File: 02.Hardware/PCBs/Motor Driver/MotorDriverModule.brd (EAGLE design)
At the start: 62 x 62 mm, 45 parts, among them Q1 DMC3021LSD-13, Q2 DMC3021LSD-13, Q3 DMC3021LSD-13, U1 FAN3268TMX, U2 FAN3268TMX, U3 FAN3268TMX, U4 MCP6001T-I_LT

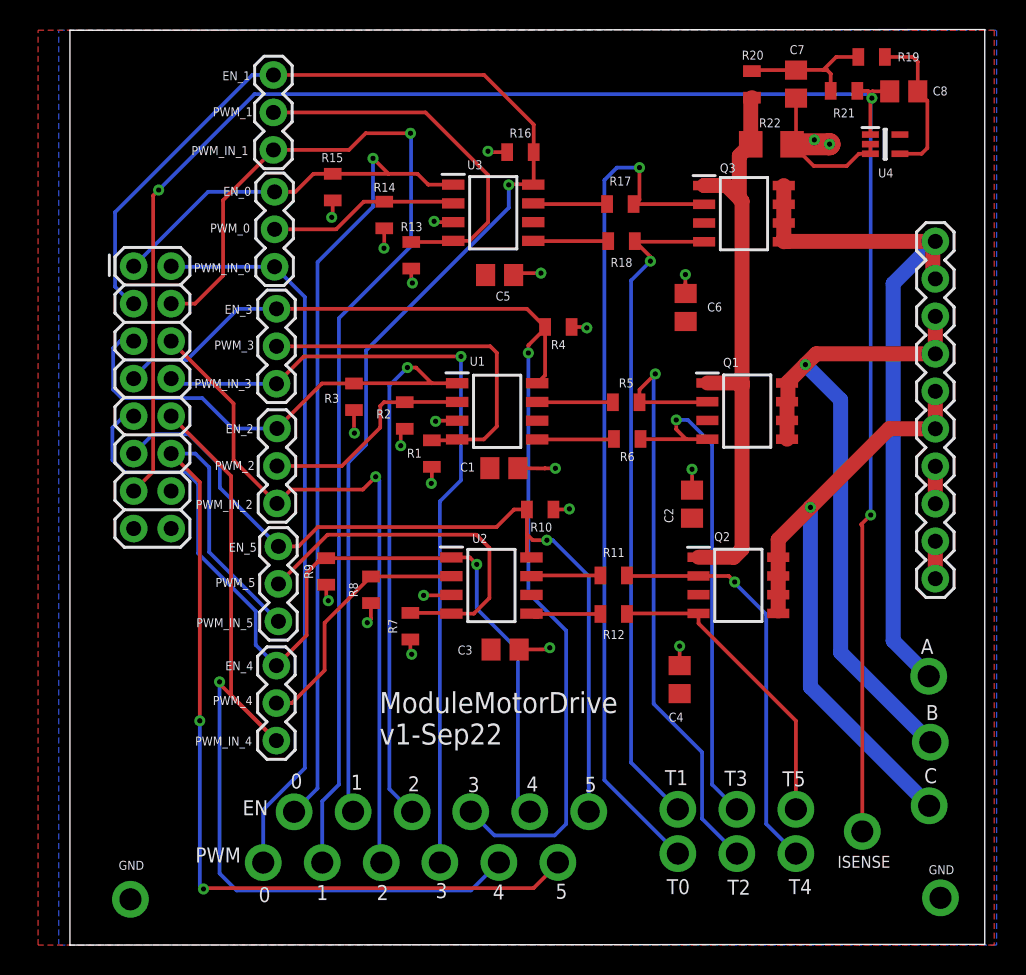
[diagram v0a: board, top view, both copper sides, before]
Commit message: Cambios de rutado y nombres
Cambios de rutado y nombres
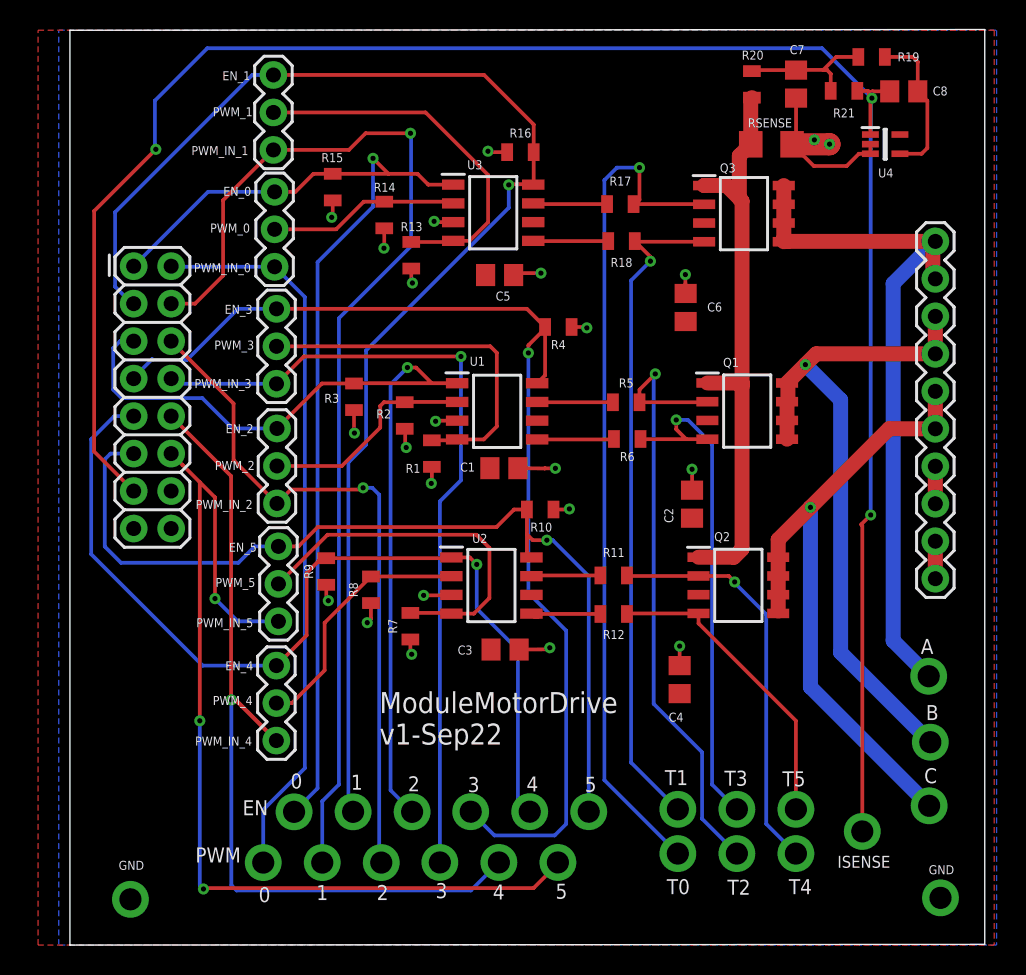
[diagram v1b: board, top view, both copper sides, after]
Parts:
- renumbered R22 to RSENSE
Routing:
- net ISENSE: track 127.9 -> 136.4 mm
- net EN_5: track 57.0 -> 63.3 mm
- net PWM_IN_4: track 63.7 -> 60.9 mm
- net PWM_IN_5: track 70.6 -> 68.5 mm, vias 3 -> 4
- net EN_4: track 62.5 -> 64.5 mm
- net PWM_IN_2: track 47.7 -> 46.5 mm

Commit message: v2 Cambio de conector de entrada y correccion de errores
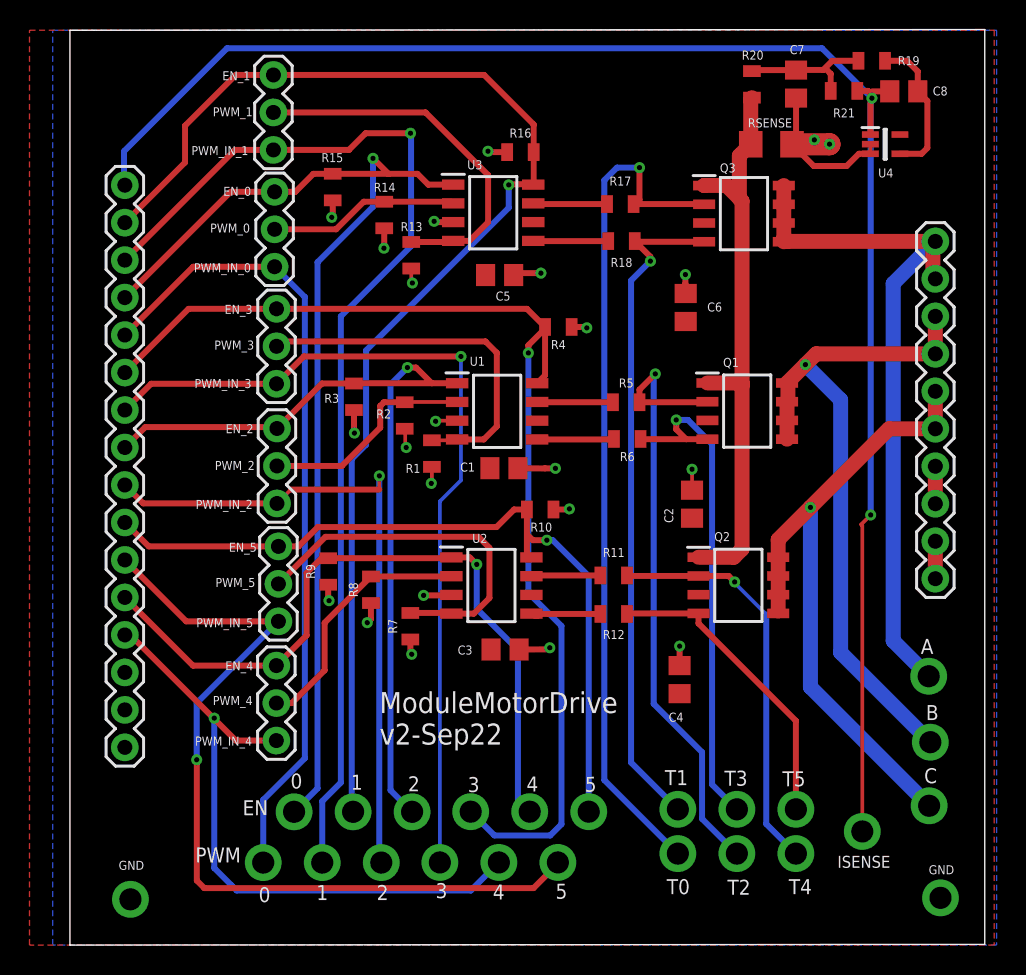
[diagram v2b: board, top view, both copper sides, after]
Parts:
- J1: device SparkFun-Connectors:2X8 -> SparkFun-Connectors:1X16
- moved J1 5.52 mm to (12.5, 58.3)
- moved R19 0.26 mm to (63.1, 66.7)
- moved R9 0.13 mm to (26.3, 32.1)
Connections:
- removed net N$27: J1.14
- net EN_0: now also J1.4; no longer J1.1
- net EN_1: now also J1.2; no longer J1.3
- net EN_2: now also J1.8; no longer J1.5
- net EN_3: now also J1.6; no longer J1.7
- net EN_4: now also J1.12; no longer J1.9
- net EN_5: now also J1.10; no longer J1.11
- net GND: now also J1.14, J1.15; no longer J1.16
- net ISENSE: now also J1.1; no longer J1.13
- net PWM_IN_0: now also J1.5; no longer J1.2
- net PWM_IN_1: now also J1.3; no longer J1.4
- net PWM_IN_2: now also J1.9; no longer J1.6
- net PWM_IN_3: now also J1.7; no longer J1.8
- net PWM_IN_4: now also J1.13; no longer J1.10
- net PWM_IN_5: now also J1.11; no longer J1.12
- net VCC: now also J1.16; no longer J1.15
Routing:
- net ISENSE: track 136.4 -> 112.9 mm, vias 4 -> 3
- net PWM_IN_4: track 60.9 -> 44.3 mm
- net EN_4: track 64.5 -> 49.7 mm
- net PWM_IN_5: track 68.5 -> 57.5 mm, vias 4 -> 2
- net EN_5: track 63.3 -> 53.7 mm
- net EN_1: track 93.3 -> 87.7 mm
- net EN_2: track 63.3 -> 57.7 mm
- net PWM_IN_0: track 49.4 -> 54.5 mm
- net PWM_IN_3: track 55.4 -> 59.2 mm
- net EN_0: track 72.5 -> 74.2 mm
- net PWM_IN_2: track 46.5 -> 45.4 mm
- net PWM_IN_1: track 75.9 -> 74.9 mm
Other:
- board text added: "ModuleMotorDrive v2-Sep22"
- board text removed: "ModuleMotorDrive v1-Sep22"

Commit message: Minor modifications
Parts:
- added C9: (no value), rcl:C0805
- moved R9 0.64 mm to (26.9, 32.2)
- moved R8 0.16 mm to (29.4, 30.9)
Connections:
- net GND: now also C9.2
- net VCC: now also C9.1
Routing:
- net A_OUT: track 59.9 -> 74.5 mm, vias 1 -> 4
- net B_OUT: track 46.4 -> 56.2 mm, vias 2 -> 4
- net EN_2: track 57.7 -> 54.7 mm
- net EN_3: track 76.9 -> 74.9 mm, vias 2 -> 3
- net PWM_IN_2: track 45.4 -> 43.6 mm
- net C_OUT: track 44.9 -> 45.7 mm, vias 2 -> 4
- net ISENSE: track 112.9 -> 113.6 mm, vias 3 -> 7
- net EN_1: track 87.7 -> 87.1 mm
- net GND: track 45.3 -> 45.9 mm, vias 25 -> 23
- net N$2: track 10.00 -> 10.4 mm, vias 0 -> 2

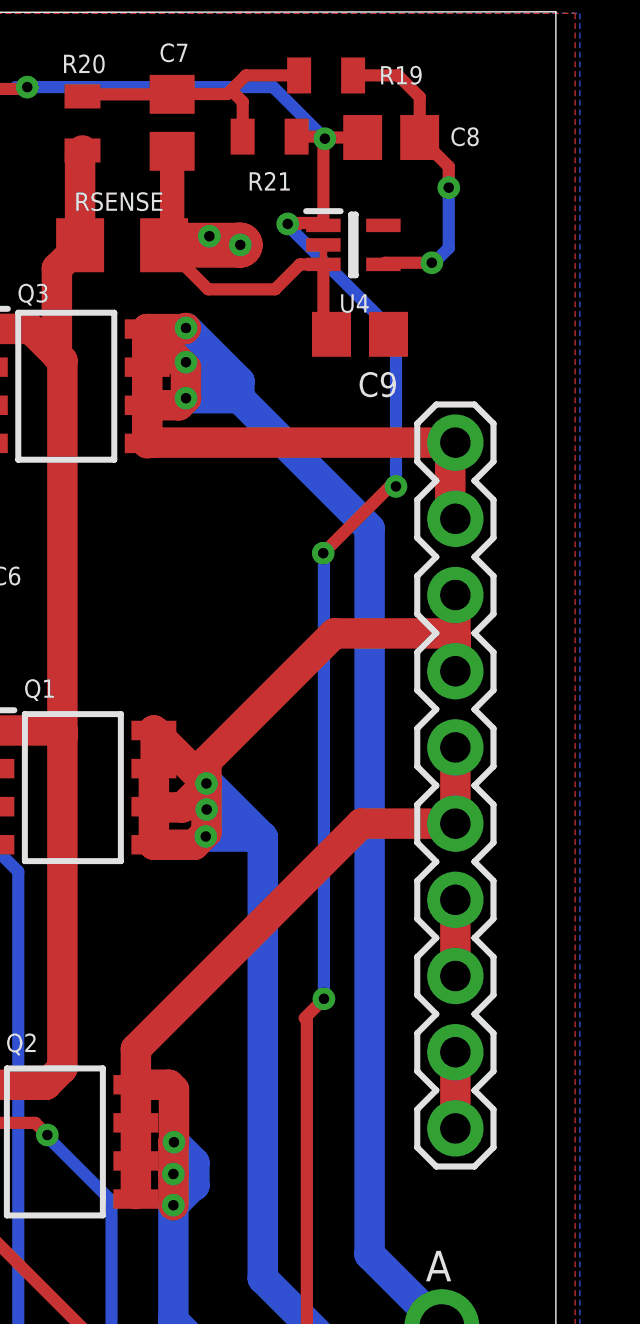
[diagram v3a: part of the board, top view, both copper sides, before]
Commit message: añadido 3v3 a driver de motor
Para que el AO filtro de ISENSE se alimente a 3v3
Se actualiza GERBER para PCBWAY
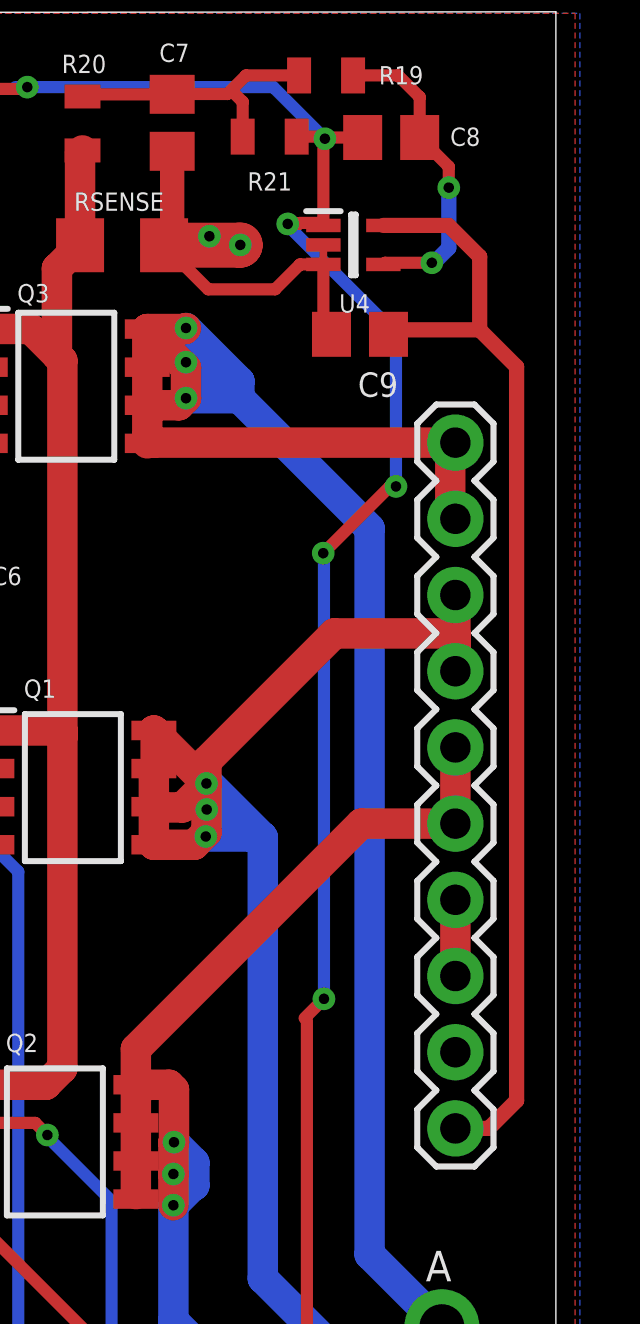
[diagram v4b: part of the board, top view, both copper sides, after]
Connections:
- new net 3V3: C9.1, J5.10, U4.5
- net GND: no longer J5.10
- net VCC: no longer C9.1, U4.5
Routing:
- net 3V3: track 0.00 -> 37.8 mm
- net GND: track 45.9 -> 43.3 mm
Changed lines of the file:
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@@
 <contactref element="U4" pad="2"/>
 <contactref element="J5" pad="9"/>
-<contactref element="J5" pad="10"/>
-<wire x1="67.45" y1="34.17" x2="67.45" y2="31.63" width="1.016" layer="1"/>
 <wire x1="63.05" y1="61.08" x2="63.05" y2="60.43" width="0.254" layer="1"/>
 <wire x1="63.05" y1="60.43" x2="62.27" y2="60.43" width="0.4064" layer="1"/>
@@
 <vertex x="71.44" y="6.8"/>
 </polygon>
-<contactref element="U4" pad="5"/>
 <contactref element="J5" pad="7"/>
 <contactref element="J5" pad="8"/>
@@
 <wire x1="67.45" y1="36.71" x2="67.45" y2="38.91" width="1.016" layer="1"/>
 <contactref element="J1" pad="16"/>
-<contactref element="C9" pad="1"/>
 </signal>
 <signal name="B_OUT">
@@
 <wire x1="67.23" y1="63.69" x2="67.23" y2="62.99" width="0.4064" layer="1"/>
 <via x="67.23" y="62.99" extent="1-16" drill="0.35"/>
-<wire x1="67.23" y1="62.99" x2="67.23" y2="60.98" width="0.4064" layer="16"/>
-<wire x1="67.23" y1="60.98" x2="66.7" y2="60.45" width="0.4064" layer="16"/>
+<wire x1="67.23" y1="62.99" x2="67.23" y2="60.98" width="0.508" layer="16"/>
+<wire x1="67.23" y1="60.98" x2="66.7" y2="60.45" width="0.508" layer="16"/>
 <wire x1="66.7" y1="60.45" x2="66.665" y2="60.485" width="0.4064" layer="16"/>
 <via x="66.665" y="60.485" extent="1-16" drill="0.35"/>
@@
 <wire x1="46.83" y1="19.17" x2="46.83" y2="51.84" width="0.4064" layer="16"/>
 </signal>
+<signal name="3V3">
+<contactref element="J5" pad="10"/>
+<contactref element="U4" pad="5"/>
+<contactref element="C9" pad="1"/>
+<wire x1="67.45" y1="31.63" x2="68.5608" y2="31.63" width="0.508" layer="1"/>
+<wire x1="68.5608" y1="31.63" x2="69.4908" y2="32.56" width="0.508" layer="1"/>
+<wire x1="69.4908" y1="57.0192" x2="68.26" y2="58.25" width="0.508" layer="1"/>
+<wire x1="68.26" y1="58.25" x2="65.37" y2="58.25" width="0.508" layer="1"/>
+<wire x1="65.37" y1="58.25" x2="65.22" y2="58.1" width="0.4064" layer="1"/>
+<wire x1="69.4908" y1="32.56" x2="69.4908" y2="57.0192" width="0.508" layer="1"/>
+<wire x1="65.05" y1="61.73" x2="67.22" y2="61.73" width="0.508" layer="1"/>
+<wire x1="68.26" y1="60.69" x2="68.26" y2="58.25" width="0.508" layer="1"/>
+<wire x1="67.22" y1="61.73" x2="68.26" y2="60.69" width="0.508" layer="1"/>
+</signal>
 </signals>

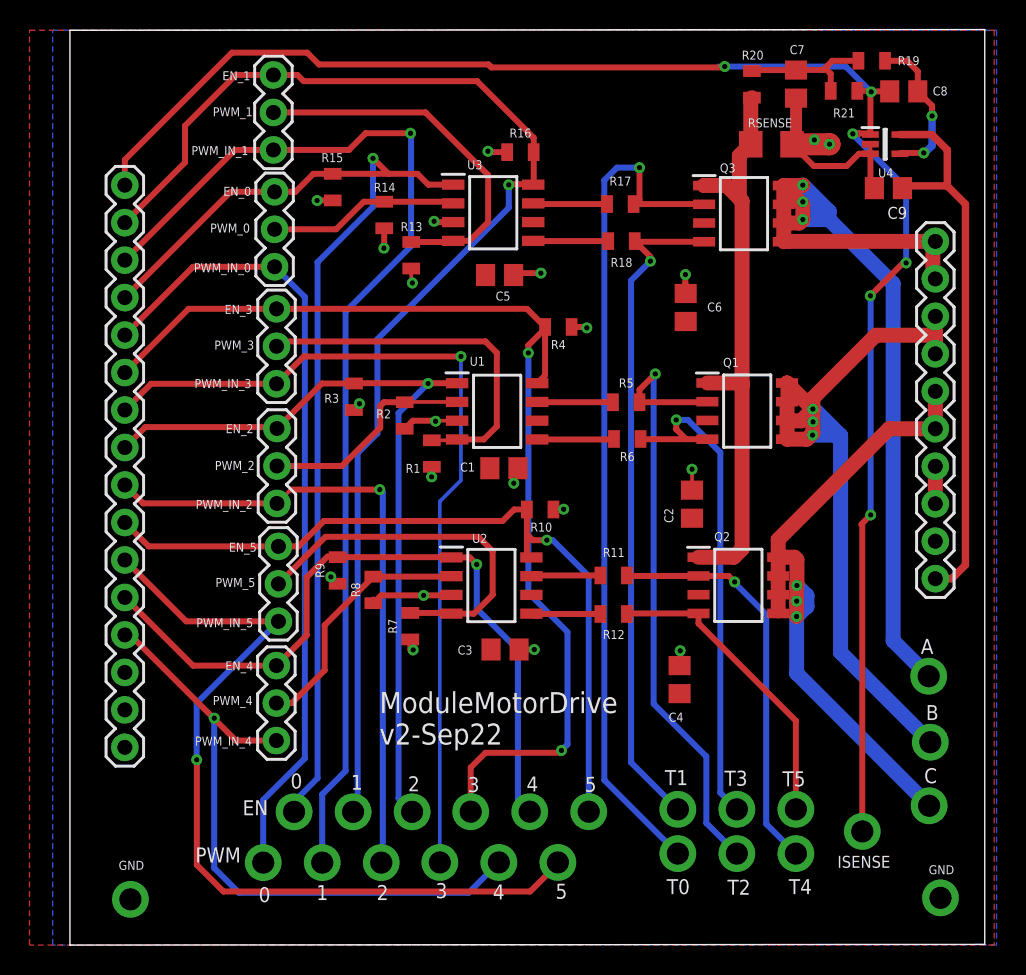
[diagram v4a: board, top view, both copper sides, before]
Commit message: Se mueve resistencia de pull-down entrada a pull-down en MOSFET
Para conseguir crear un tDEAD entre transistores
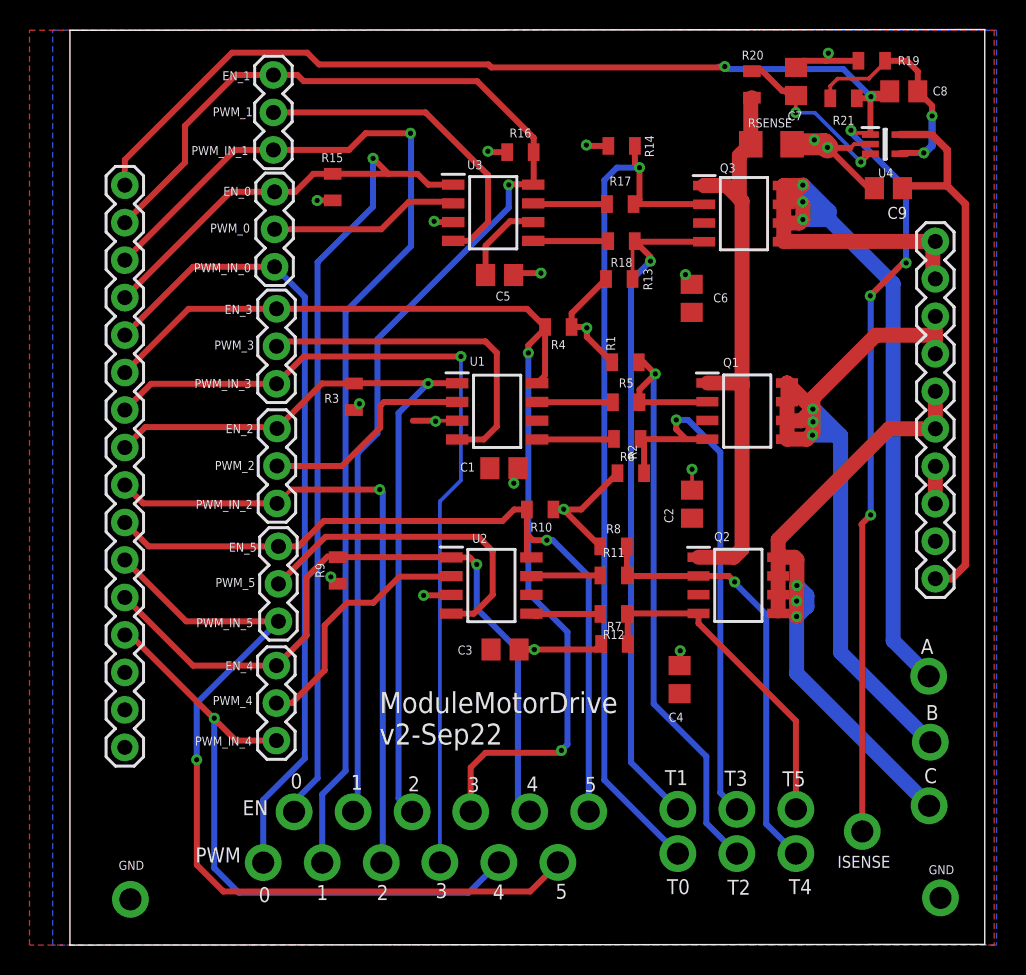
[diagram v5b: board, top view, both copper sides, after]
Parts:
- moved R14 16.8 mm to (46.2, 61.0), turned to 0 degrees
- moved R8 16.5 mm to (45.6, 33.8), turned to 0 degrees
- moved R2 15.8 mm to (46.8, 38.8), turned to 0 degrees
- moved R1 14.5 mm to (46.5, 46.3), turned to 0 degrees
- moved R13 14.2 mm to (46.0, 51.9), turned to 0 degrees
- moved R7 13.9 mm to (45.7, 27.2), turned to 0 degrees
- moved C6 0.74 mm to (50.9, 50.6)
- moved R21 0.50 mm to (61.2, 64.2)
- moved C7 0.18 mm to (58.0, 65.3), turned to 90 degrees
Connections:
- removed net N$1: C7.1, R19.2, R20.1, R21.2
- new net N$3: C7.1, R20.1, U4.3
- net GND: now also R19.2; no longer U4.3
- net N$2: now also R21.2
- net PWM_0: no longer R14.2
- net PWM_1: no longer R13.2
- net PWM_2: no longer R2.2
- net PWM_3: no longer R1.2
- net PWM_4: no longer R8.2
- net PWM_5: no longer R7.2
- net T0: now also R14.2
- net T1: now also R13.2
- net T2: now also R1.2
- net T3: now also R2.2
- net T4: now also R8.2
- net T5: now also R7.2
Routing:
- net GND: track 43.3 -> 59.5 mm, vias 23 -> 21
- net N$3: track 0.00 -> 11.9 mm, vias 0 -> 2
- net N$1: track 9.30 -> 0.00 mm
- net VCC: track 2.54 -> 8.48 mm
- net N$2: track 10.4 -> 15.7 mm
- net PWM_1: track 25.3 -> 22.5 mm
- net PWM_5: track 25.3 -> 22.6 mm
- net T1: track 45.5 -> 48.2 mm
- net T3: track 34.7 -> 37.1 mm
- net T5: track 20.9 -> 22.9 mm
- net T4: track 27.6 -> 29.6 mm
- net ISENSE: track 113.6 -> 115.4 mm
- net PWM_3: track 25.2 -> 23.5 mm
- net T0: track 57.8 -> 59.4 mm
- net T2: track 41.9 -> 43.3 mm
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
